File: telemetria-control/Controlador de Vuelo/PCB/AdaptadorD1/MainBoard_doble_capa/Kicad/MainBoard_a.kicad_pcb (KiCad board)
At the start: 2 copper layers, 45 x 45 mm, 14 parts, among them J1 Conn_01x04, J2 Conn_01x05, J3 Conn_01x02, J4 Conn_01x08, J5 Conn_01x08, Q1 BC548, U1 WeMos_mini, U2 4066

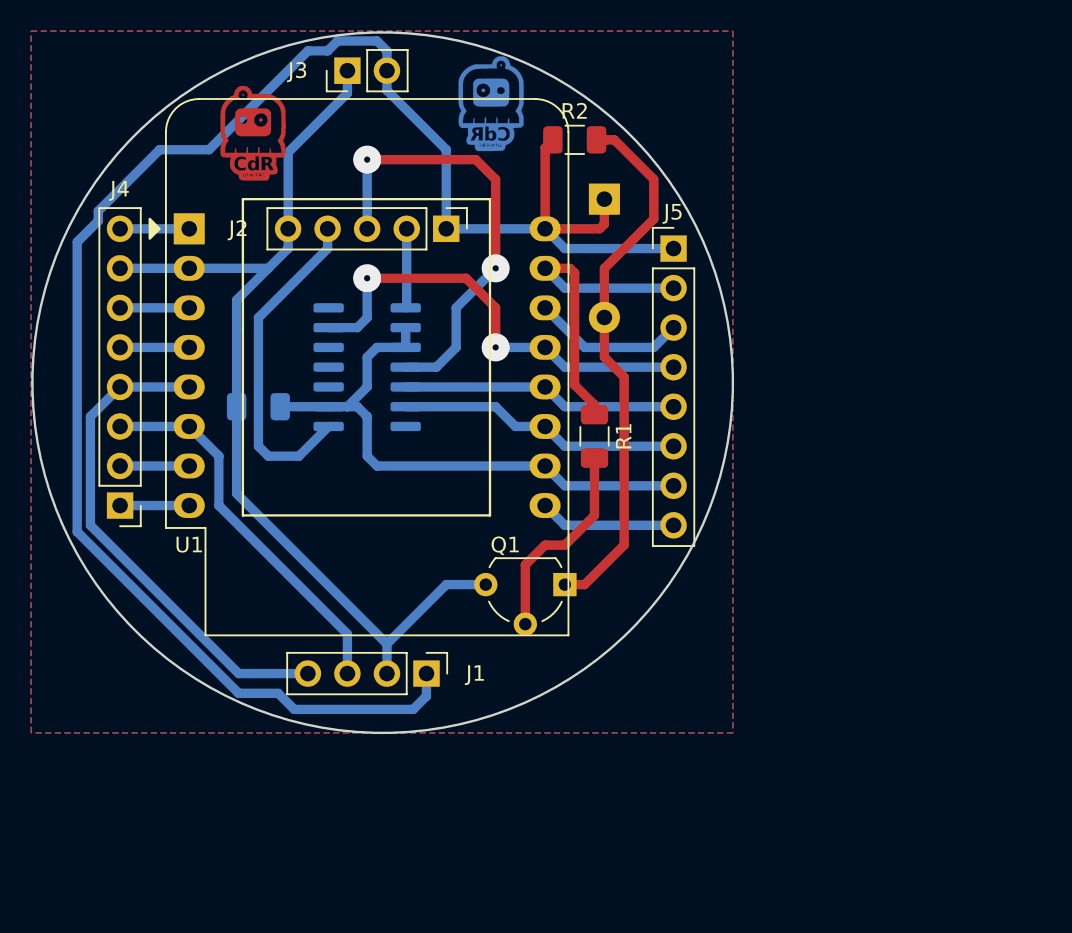
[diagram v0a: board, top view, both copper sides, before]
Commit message: Se modificaron los tamaños de algunos pads en kicad y se reimprimieron los archivos de PCB
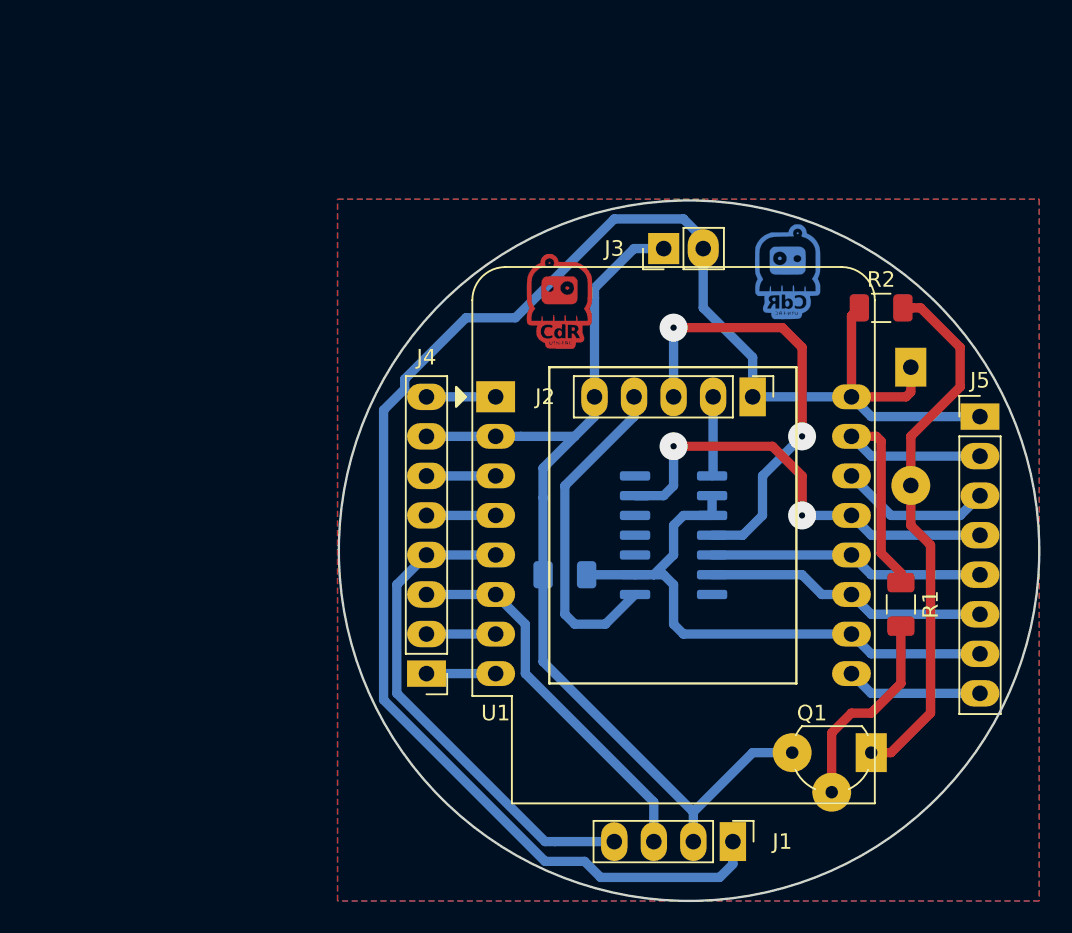
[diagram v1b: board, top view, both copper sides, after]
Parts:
- moved J3 23.3 mm to (166.4, 86.4)
- moved ? 22.5 mm to (160.0, 89.5)
- moved BZ1 22.5 mm to (182.2, 94.0)
- moved J2 22.5 mm to (172.1, 95.9)
- moved J4 22.5 mm to (151.1, 113.7)
- moved J5 22.5 mm to (186.7, 97.2)
- moved Q1 22.5 mm to (179.7, 118.7)
- moved R1 22.5 mm to (181.6, 109.2)
- moved R2 22.5 mm to (180.3, 90.2)
- moved R3 22.5 mm to (160.0, 107.3)
- moved U1 22.5 mm to (155.6, 95.9)
- moved U2 22.5 mm to (167.0, 104.8)
- moved J1 22.5 mm to (170.8, 124.5)
- moved ? 21.9 mm to (174.0, 87.6)
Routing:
- net 3v3: track 113.1 -> 112.2 mm
- net GND: track 63.1 -> 63.9 mm
